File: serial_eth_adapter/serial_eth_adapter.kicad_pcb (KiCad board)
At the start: 2 copper layers, 0 parts

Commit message: feat(serial_eth_adapter): add PCB placement and partial routing
Problem: The PCB only contained unplaced footprints synced from the schematic, so there was no
board outline, placement or copper to review.

Solution: Placed all 119 footprints on a 72 x 92 mm 2-layer board (Ethernet on the top edge, serial
connectors on the bottom edge, isolation gap across the middle), added GND and GND_ISO planes on the
bottom layer, set net classes and 0.15 mm rules, swapped the reverse-polarity FET to a 40 V part, and
applied about two thirds of the Freerouting result as traces and vias. The router inputs and log are
kept in route/.

Testing: Placement scores 70 with no hard failures; DRC and the remaining routing are not done yet,
so this board is not ready for fabrication.

Co-Authored-By: Claude Sonnet 5.5 <noreply@anthropic.com>
Claude-Session: https://claude.ai/code/session_01Aw9LDF5oz5X6KBMNcxHCBZ
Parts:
- added C1: 47uF 50V, Capacitor_SMD:CP_Elec_6.3x7.7, F.Cu at (68.0, 75.0)
- added C10: 15pF, Capacitor_SMD:C_0603_1608Metric, F.Cu at (99.5, 86.0)
- added C11: 15pF, Capacitor_SMD:C_0603_1608Metric, F.Cu at (108.5, 86.0)
- added C12: 100nF, Capacitor_SMD:C_0603_1608Metric, F.Cu at (99.5, 66.6)
- added C13: 100nF, Capacitor_SMD:C_0603_1608Metric, F.Cu at (102.8, 66.6)
- added C14: 100nF, Capacitor_SMD:C_0603_1608Metric, F.Cu at (106.1, 66.6)
- added C15: 100nF, Capacitor_SMD:C_0603_1608Metric, F.Cu at (109.4, 66.6)
- added C16: 100nF, Capacitor_SMD:C_0603_1608Metric, F.Cu at (100.0, 80.0)
- added C17: 100nF, Capacitor_SMD:C_0603_1608Metric, F.Cu at (108.0, 80.0)
- added C18: 100nF, Capacitor_SMD:C_0603_1608Metric, F.Cu at (96.8, 70.0)
- added C19: 100nF, Capacitor_SMD:C_0603_1608Metric, F.Cu at (96.8, 73.3)
- added C2: 10uF 50V, Capacitor_SMD:C_1206_3216Metric, F.Cu at (75.5, 72.5)
- added C20: 1uF, Capacitor_SMD:C_0603_1608Metric, F.Cu at (96.8, 76.6)
- added C21: 1uF, Capacitor_SMD:C_0603_1608Metric, F.Cu at (111.2, 70.0)
- added C22: 100nF, Capacitor_SMD:C_0603_1608Metric, F.Cu at (111.2, 73.3)
- added C23: 100nF, Capacitor_SMD:C_0603_1608Metric, F.Cu at (111.2, 76.6)
- added C24: 100nF, Capacitor_SMD:C_0603_1608Metric, F.Cu at (104.0, 80.0)
- added C25: 100nF, Capacitor_SMD:C_0603_1608Metric, F.Cu at (95.0, 66.5)
- added C3: 100nF, Capacitor_SMD:C_0603_1608Metric, F.Cu at (74.0, 86.2)
- added C30: 18pF, Capacitor_SMD:C_0603_1608Metric, F.Cu at (118.5, 84.0)
- added C31: 18pF, Capacitor_SMD:C_0603_1608Metric, F.Cu at (127.5, 84.0)
- added C32: 4.7uF, Capacitor_SMD:C_0603_1608Metric, F.Cu at (119.5, 78.0)
- added C33: 10nF, Capacitor_SMD:C_0603_1608Metric, F.Cu at (123.0, 78.0)
- added C34: 10uF, Capacitor_SMD:C_0603_1608Metric, F.Cu at (126.5, 78.0)
- added C35: 100nF, Capacitor_SMD:C_0603_1608Metric, F.Cu at (115.5, 66.5)
- added C36: 100nF, Capacitor_SMD:C_0603_1608Metric, F.Cu at (115.5, 69.8)
- added C37: 100nF, Capacitor_SMD:C_0603_1608Metric, F.Cu at (115.5, 73.1)
- added C38: 100nF, Capacitor_SMD:C_0603_1608Metric, F.Cu at (115.5, 76.4)
- added C39: 100nF, Capacitor_SMD:C_0603_1608Metric, F.Cu at (130.2, 66.5)
- added C4: 22uF 25V, Capacitor_SMD:C_0805_2012Metric, F.Cu at (79.5, 88.0)
- added C40: 100nF, Capacitor_SMD:C_0603_1608Metric, F.Cu at (130.2, 69.8)
- added C5: 22uF 25V, Capacitor_SMD:C_0805_2012Metric, F.Cu at (83.5, 88.0)
- added C50: 100nF, Capacitor_SMD:C_0603_1608Metric, F.Cu at (84.0, 91.5)
- added C51: 100nF, Capacitor_SMD:C_0603_1608Metric, F.Cu at (84.0, 102.5)
- added C52: 100nF, Capacitor_SMD:C_0603_1608Metric, F.Cu at (92.5, 91.5)
- added C53: 100nF, Capacitor_SMD:C_0603_1608Metric, F.Cu at (92.5, 102.5)
- added C54: 100nF, Capacitor_SMD:C_0603_1608Metric, F.Cu at (101.0, 91.5)
- added C55: 100nF, Capacitor_SMD:C_0603_1608Metric, F.Cu at (101.0, 102.5)
- added C56: 100nF, Capacitor_SMD:C_0603_1608Metric, F.Cu at (109.5, 91.5)
- added C57: 100nF, Capacitor_SMD:C_0603_1608Metric, F.Cu at (109.5, 102.5)
- added C58: 4.7uF, Capacitor_SMD:C_0603_1608Metric, F.Cu at (64.0, 92.5)
- added C59: 10uF, Capacitor_SMD:C_0603_1608Metric, F.Cu at (64.0, 100.0)
- added C60: 100nF, Capacitor_SMD:C_0603_1608Metric, F.Cu at (106.0, 110.0)
- added C61: 100nF, Capacitor_SMD:C_0603_1608Metric, F.Cu at (106.0, 112.5)
- added C62: 100nF, Capacitor_SMD:C_0603_1608Metric, F.Cu at (65.0, 105.5)
- added C63: 100nF, Capacitor_SMD:C_0603_1608Metric, F.Cu at (65.0, 108.9)
- added C64: 100nF, Capacitor_SMD:C_0603_1608Metric, F.Cu at (62.2, 105.5)
- added C65: 100nF, Capacitor_SMD:C_0603_1608Metric, F.Cu at (62.2, 108.9)
- added C66: 100nF, Capacitor_SMD:C_0603_1608Metric, F.Cu at (71.5, 112.2)
- added C67: 100nF, Capacitor_SMD:C_0603_1608Metric, F.Cu at (85.0, 112.2)
- added D1: BZT52C10 (10V), Diode_SMD:D_SOD-123, F.Cu at (81.5, 66.5)
- added D10: SMAJ15CA, Diode_SMD:D_SMA, F.Cu at (65.5, 116.2)
- added D11: SMAJ15CA, Diode_SMD:D_SMA, F.Cu at (73.2, 116.2)
- added D12: SMAJ15CA, Diode_SMD:D_SMA, F.Cu at (80.9, 116.2)
- added D13: SMAJ15CA, Diode_SMD:D_SMA, F.Cu at (88.6, 116.2)
- added D14: PSM712, Package_TO_SOT_SMD:SOT-23, F.Cu at (106.0, 106.0)
- added D2: SMBJ33A, Diode_SMD:D_SMB, F.Cu at (67.5, 66.5)
- added D3: LED red, LED_SMD:LED_0603_1608Metric, F.Cu at (64.0, 83.0)
- added D4: LED red STATUS, LED_SMD:LED_0603_1608Metric, F.Cu at (89.5, 74.0)
- added D5: LED red ERR, LED_SMD:LED_0603_1608Metric, F.Cu at (89.5, 80.0)
- added F1: 1.1A 33V PTC, Fuse:Fuse_1812_4532Metric, F.Cu at (74.0, 59.5)
- added FB1: FB 100R@100MHz, Inductor_SMD:L_0805_2012Metric, F.Cu at (130.2, 73.5)
- added J1: VIN 5-32V (5.08mm), Connector_Phoenix_MSTB:PhoenixContact_MSTBA_2,5_2-G-5,08_1x02_P5.08mm_Horizontal, F.Cu at (74.0, 50.5)
- added J2: USB-C, Connector_USB:USB_C_Receptacle_HRO_TYPE-C-31-M-12, F.Cu at (90.0, 43.9)
- added J3: SWD (CLK,GND,DIO), Connector_PinHeader_2.54mm:PinHeader_1x03_P2.54mm_Vertical, F.Cu at (88.5, 86.5)
- added J4: HR911105A, Connector_RJ:RJ45_Hanrun_HR911105A_Horizontal, F.Cu at (126.5, 52.5)
- added J5: DB9 male (DTE), Connector_Dsub:DSUB-9_Pins_Horizontal_P2.77x2.84mm_EdgePinOffset7.70mm_Housed_MountingHolesOffset9.12mm, F.Cu at (71.9, 121.5)
- added J6: Serial 5-pos (5.08mm), Connector_Phoenix_MSTB:PhoenixContact_MSTBA_2,5_5-G-5,08_1x05_P5.08mm_Horizontal, F.Cu at (101.5, 121.5)
- added JP1: TERM 120R (solder bridge), Jumper:SolderJumper-2_P1.3mm_Open_Pad1.0x1.5mm, F.Cu at (100.8, 106.0)
- added JP2: BIAS A pull-up (solder bridge), Jumper:SolderJumper-2_P1.3mm_Open_Pad1.0x1.5mm, F.Cu at (100.8, 109.0)
- added JP3: BIAS B pull-down (solder bridge), Jumper:SolderJumper-2_P1.3mm_Open_Pad1.0x1.5mm, F.Cu at (100.8, 112.0)
- added JP4: MODE override: 1=RS232 2=ctr 3=RS485, Jumper:SolderJumper-3_P1.3mm_Open_Pad1.0x1.5mm_NumberLabels, F.Cu at (125.0, 107.0)
- added L1: 3.9uH 2.1A, Inductor_SMD:L_Sunlord_SWPA4030S, F.Cu at (82.0, 82.5)
- added PS1: B0303S-1WR3, serial_eth:SIP-4_B0303S-1WR3_11.6x6mm_P2.54mm, F.Cu at (69.0, 92.0)
- added Q1: DMP4065S-7, Package_TO_SOT_SMD:SOT-23, F.Cu at (75.0, 66.5)
- added R1: 10k, Resistor_SMD:R_0603_1608Metric, F.Cu at (81.5, 69.5)
- added R10: 1k, Resistor_SMD:R_0603_1608Metric, F.Cu at (104.0, 82.9)
- added R11: 27, Resistor_SMD:R_0603_1608Metric, F.Cu at (90.0, 52.6)
- added R12: 27, Resistor_SMD:R_0603_1608Metric, F.Cu at (90.0, 54.4)
- added R13: 5.1k, Resistor_SMD:R_0603_1608Metric, F.Cu at (95.5, 51.5)
- added R14: 5.1k, Resistor_SMD:R_0603_1608Metric, F.Cu at (84.5, 51.5)
- added R15: 1k, Resistor_SMD:R_0603_1608Metric, F.Cu at (95.2, 61.0)
- added R17: 330, Resistor_SMD:R_0603_1608Metric, F.Cu at (89.5, 77.0)
- added R18: 330, Resistor_SMD:R_0603_1608Metric, F.Cu at (89.5, 83.0)
- added R2: 330, Resistor_SMD:R_0603_1608Metric, F.Cu at (64.0, 86.0)
- added R20: 1M, Resistor_SMD:R_0603_1608Metric, F.Cu at (119.5, 80.5)
- added R21: 0, Resistor_SMD:R_0603_1608Metric, F.Cu at (126.5, 80.5)
- added R22: 12.4k 1%, Resistor_SMD:R_0603_1608Metric, F.Cu at (130.2, 78.0)
- added R23: 330, Resistor_SMD:R_0603_1608Metric, F.Cu at (110.5, 46.5)
- added R24: 330, Resistor_SMD:R_0603_1608Metric, F.Cu at (110.5, 43.5)
- added R30: 10k, Resistor_SMD:R_0603_1608Metric, F.Cu at (88.3, 91.5)
- added R31: 10k, Resistor_SMD:R_0603_1608Metric, F.Cu at (96.8, 91.5)
- added R32: 10k, Resistor_SMD:R_0603_1608Metric, F.Cu at (105.3, 91.5)
- added R33: 10k, Resistor_SMD:R_0603_1608Metric, F.Cu at (113.8, 91.5)
- added R40: 120, Resistor_SMD:R_0603_1608Metric, F.Cu at (96.5, 106.0)
- added R41: 680, Resistor_SMD:R_0603_1608Metric, F.Cu at (96.5, 109.0)
- added R42: 680, Resistor_SMD:R_0603_1608Metric, F.Cu at (96.5, 112.0)
- added R43: 10k, Resistor_SMD:R_0603_1608Metric, F.Cu at (125.0, 111.0)
- added R44: 150, Resistor_SMD:R_0603_1608Metric, F.Cu at (74.5, 100.0)
- added R45: 10, Resistor_SMD:R_0603_1608Metric, F.Cu at (91.5, 106.0)
- added R46: 10, Resistor_SMD:R_0603_1608Metric, F.Cu at (91.5, 109.0)
- added R47: 100k, Resistor_SMD:R_0603_1608Metric, F.Cu at (112.5, 111.0)
- added R48: 1k, Resistor_SMD:R_0603_1608Metric, F.Cu at (118.5, 111.0)
- added SW1: BOOTSEL, serial_eth:SW_TS-1187A_5.1x5.1mm, F.Cu at (89.0, 61.5)
- added SW2: RESET (RUN), serial_eth:SW_TS-1187A_5.1x5.1mm, F.Cu at (89.0, 67.5)
- added U1: AP63203WU-7, Package_TO_SOT_SMD:TSOT-23-6, F.Cu at (74.0, 82.0)
- added U10: 74LVC2G32, Package_SO:VSSOP-8_2.3x2mm_P0.5mm, F.Cu at (118.5, 107.0)
- added U11: SP3232EEY, Package_SO:TSSOP-16_4.4x5mm_P0.65mm, F.Cu at (71.5, 107.5)
- added U12: SN65HVD72DR, Package_SO:SOIC-8_3.9x4.9mm_P1.27mm, F.Cu at (85.0, 107.5)
- added U2: RP2040, Package_DFN_QFN:QFN-56-1EP_7x7mm_P0.4mm_EP3.2x3.2mm, F.Cu at (104.0, 73.0)
- added U3: W25Q16JVSSIQ, Package_SO:SOIC-8_5.3x5.3mm_P1.27mm, F.Cu at (104.0, 59.0)
- added U4: W5500, Package_QFP:LQFP-48_7x7mm_P0.5mm, F.Cu at (123.0, 70.0)
- added U5: ADuM1201ARZ, Package_SO:SOIC-8_3.9x4.9mm_P1.27mm, F.Cu at (84.0, 97.0)
- added U6: ADuM1201ARZ, Package_SO:SOIC-8_3.9x4.9mm_P1.27mm, F.Cu at (92.5, 97.0)
- added U7: ADuM1201ARZ, Package_SO:SOIC-8_3.9x4.9mm_P1.27mm, F.Cu at (101.0, 97.0)
- added U8: ADuM1201ARZ, Package_SO:SOIC-8_3.9x4.9mm_P1.27mm, F.Cu at (109.5, 97.0)
- added U9: 74LVC1G08, Package_TO_SOT_SMD:SOT-23-5, F.Cu at (112.5, 107.0)
- added Y1: 12MHz 10pF, Crystal:Crystal_SMD_3225-4Pin_3.2x2.5mm, F.Cu at (104.0, 86.0)
- added Y2: 25MHz 18pF, Crystal:Crystal_SMD_3225-4Pin_3.2x2.5mm, F.Cu at (123.0, 84.0)
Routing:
- net +3V3: track 0.00 -> 242.5 mm, vias 0 -> 3
- net +3V3_ISO: track 0.00 -> 136.2 mm
- net GND: track 0.00 -> 126.3 mm, vias 0 -> 79
- net RS485_B: track 0.00 -> 81.8 mm, vias 0 -> 1
- net GND_ISO: track 0.00 -> 62.9 mm, vias 0 -> 35
- net /Isolation + Serial/RXD485_ISO: track 0.00 -> 58.6 mm, vias 0 -> 2
- net RS232_RXD: track 0.00 -> 57.8 mm
- net /Isolation + Serial/TXD_ISO: track 0.00 -> 48.2 mm, vias 0 -> 2
- net /Power/VIN_PROT: track 0.00 -> 43.7 mm
- net /Ethernet/+3V3A: track 0.00 -> 43.5 mm, vias 0 -> 2
- net UART_TXD: track 0.00 -> 37.7 mm, vias 0 -> 2
- net /Isolation + Serial/DE_RE: track 0.00 -> 33.6 mm, vias 0 -> 2
- net /Isolation + Serial/MODE_ISO: track 0.00 -> 30.8 mm, vias 0 -> 2
- net RS232_RTS: track 0.00 -> 29.3 mm, vias 0 -> 1
- net /MCU/QSPI_SS: track 0.00 -> 22.6 mm
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- added copper zone on B.Cu, net GND
- added copper zone on B.Cu, net GND_ISO
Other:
- board outline added: 72 x 92 mm

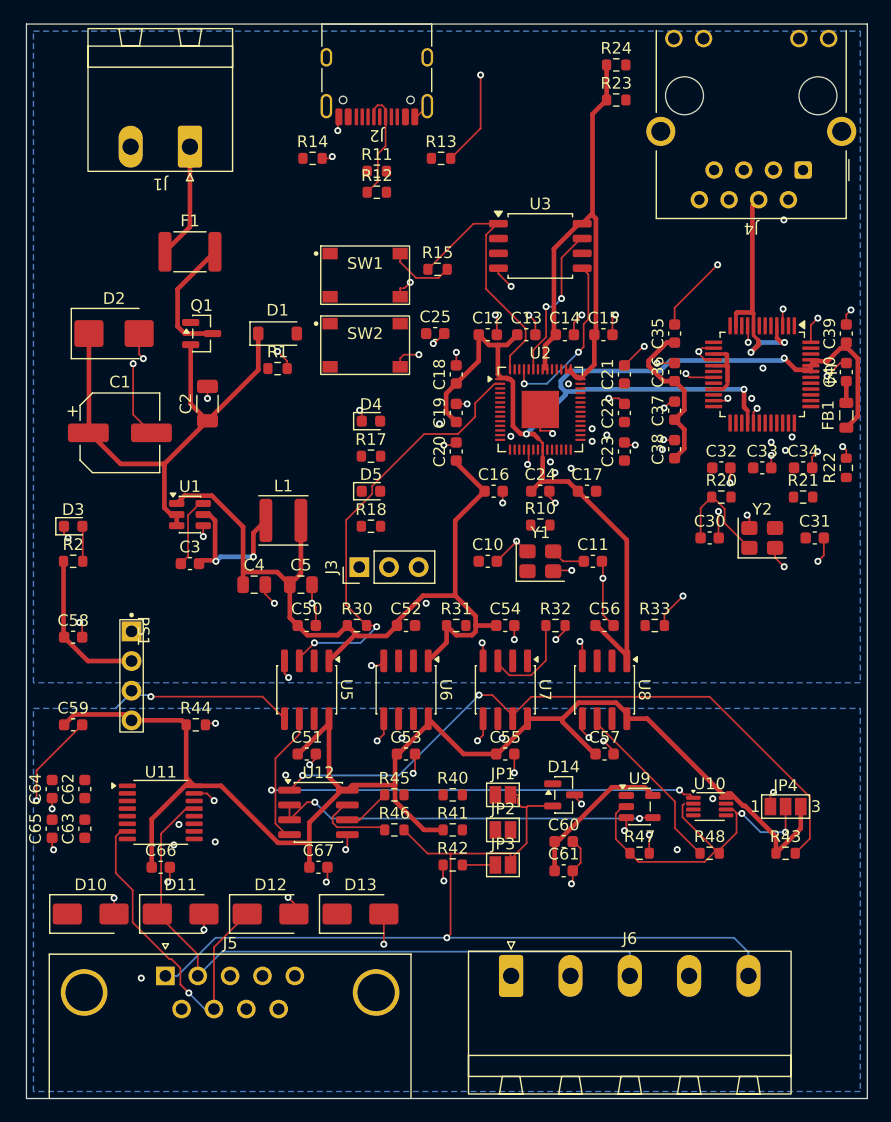
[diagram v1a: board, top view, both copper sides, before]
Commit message: feat(serial_eth_adapter): apply autorouter result to the PCB
Problem: The board had placement and planes but no signal routing, so it could not be checked for
manufacturing.

Solution: Applied the Freerouting result (about 1000 tracks and 137 vias) through the KiCad tools
and restored the 0.15 mm Default and Power net classes after KiCad overwrote them.

Testing: DRC reports no clearance violations; 40 unconnected items, 4 board-edge errors and 8
solder-jumper mask warnings remain to be fixed.

Co-Authored-By: Claude Sonnet 5.5 <noreply@anthropic.com>
Claude-Session: https://claude.ai/code/session_01Aw9LDF5oz5X6KBMNcxHCBZ
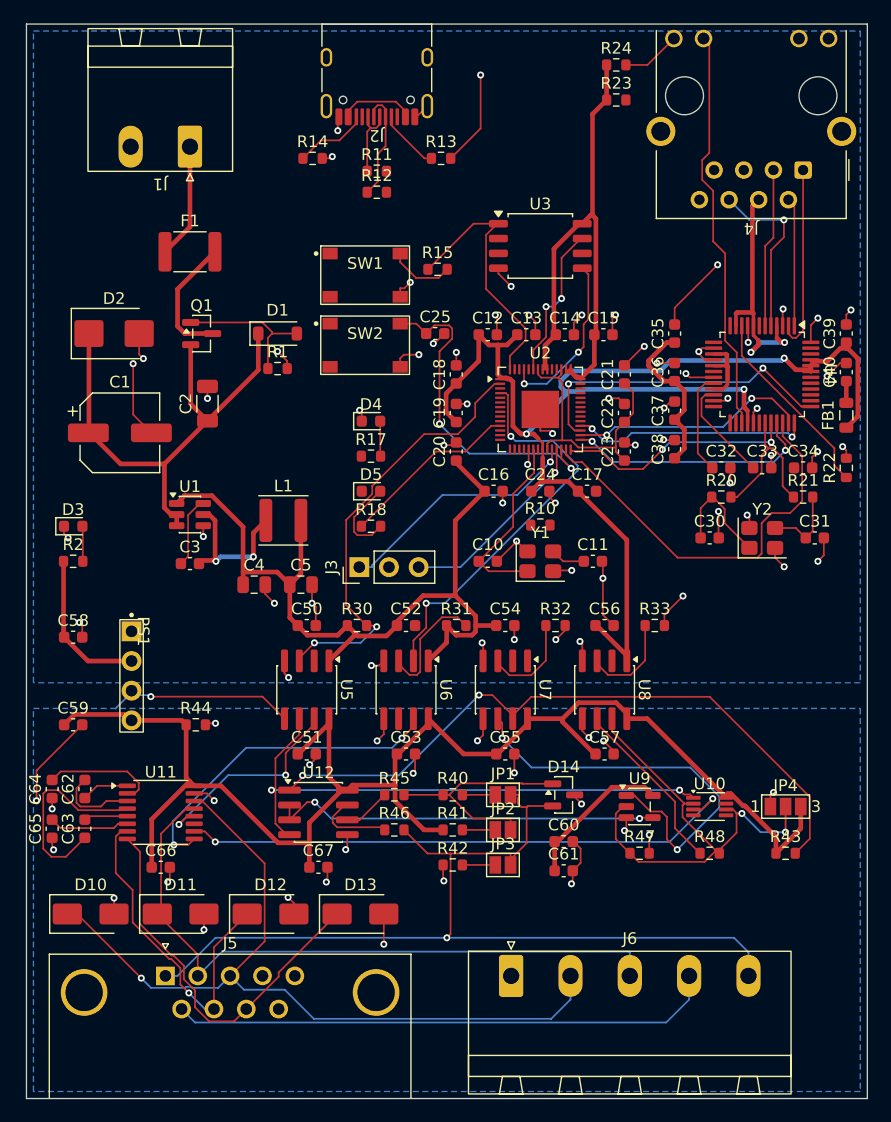
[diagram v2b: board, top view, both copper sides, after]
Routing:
- net RS232_TXD: track 0.00 -> 69.5 mm, vias 0 -> 1
- net RS485_A: track 0.00 -> 67.0 mm
- net /Isolation + Serial/T2IN_232: track 0.00 -> 48.4 mm, vias 0 -> 2
- net /Isolation + Serial/DIR_ISO: track 0.00 -> 35.9 mm, vias 0 -> 2
- net W5500_MISO: track 0.00 -> 35.2 mm
- net /Ethernet/ACT_LED_K: track 0.00 -> 34.8 mm
- net UART_CTS: track 0.00 -> 34.6 mm, vias 0 -> 2
- net RS232_CTS: track 0.00 -> 33.6 mm
- net /Isolation + Serial/CTS_ISO: track 0.00 -> 28.7 mm, vias 0 -> 2
- net /MCU/RUN: track 0.00 -> 28.6 mm, vias 0 -> 2
- net W5500_RST: track 0.00 -> 27.4 mm, vias 0 -> 2
- net /MCU/DVDD_1V1: track 0.00 -> 23.2 mm
- net W5500_SCK: track 0.00 -> 21.4 mm, vias 0 -> 2
- net /MCU/SWCLK: track 0.00 -> 21.3 mm, vias 0 -> 1
- net W5500_CS: track 0.00 -> 20.5 mm, vias 0 -> 2
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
